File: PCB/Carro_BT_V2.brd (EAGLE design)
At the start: 58 x 71 mm, 7 parts, among them X2 22-23-2041, X3 22-23-2021, X4 22-23-2021

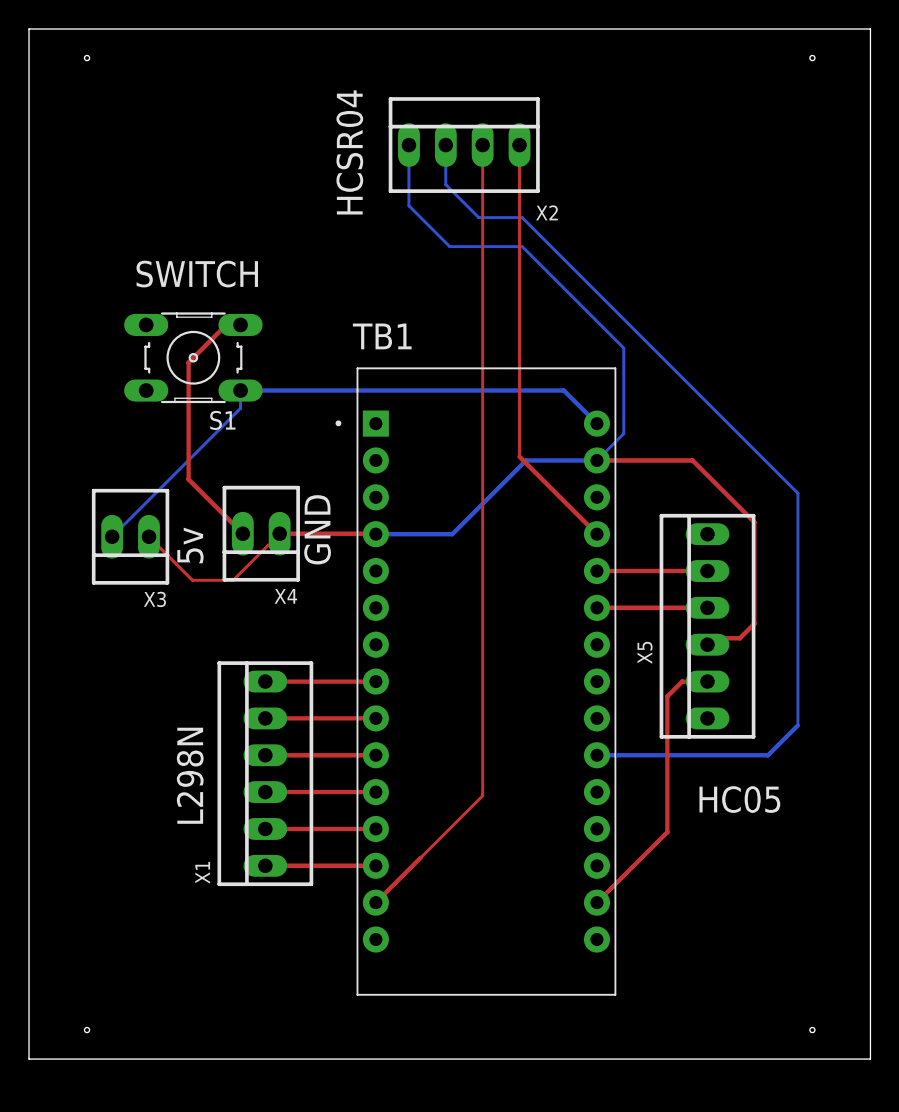
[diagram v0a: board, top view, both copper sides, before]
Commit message: Se reduce el tamaño de la PCB para reducir el precio de fabricación.
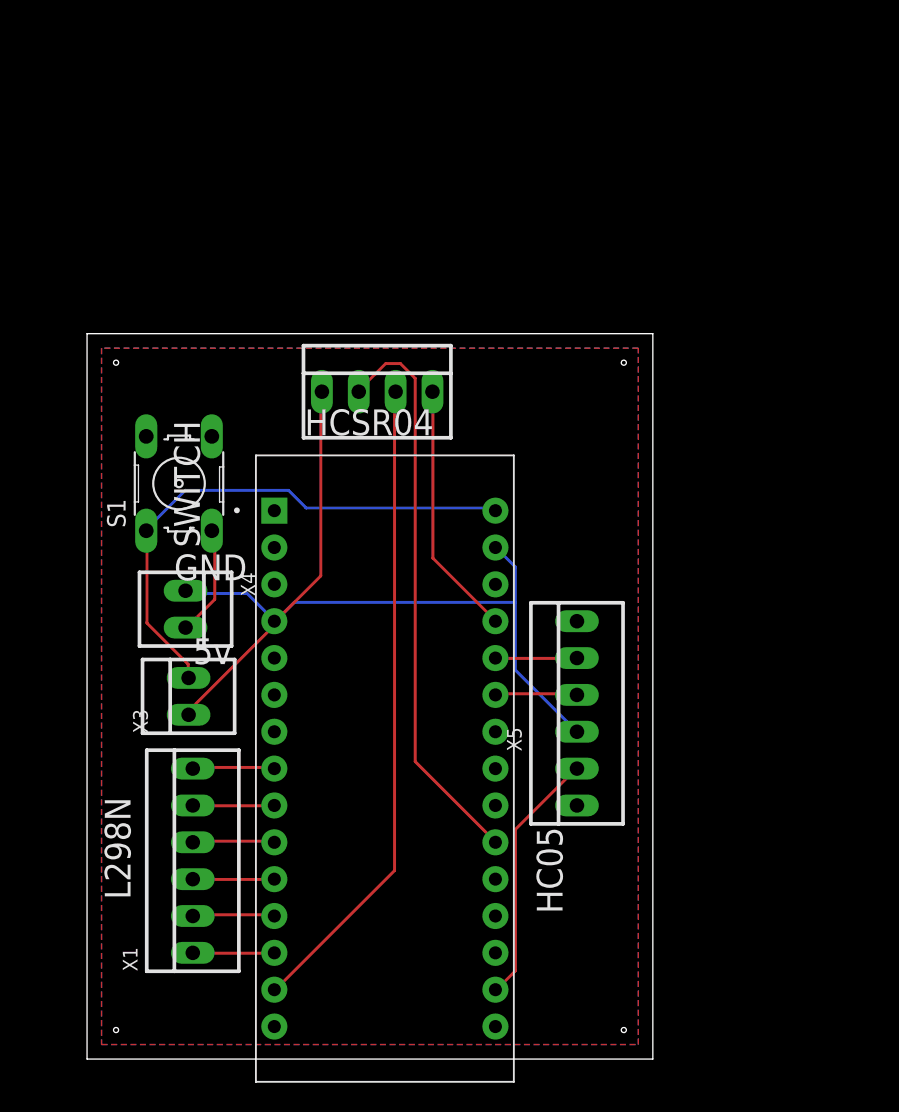
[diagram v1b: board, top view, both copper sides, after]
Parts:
- moved X2 18.0 mm to (24.0, 46.0)
- moved X3 11.7 mm to (11.0, 25.0), turned to 90 degrees
- moved X5 10.8 mm to (37.8, 23.8)
- moved TB1 9.22 mm to (24.5, 20.0)
- moved S1 8.73 mm to (10.3, 39.7), turned to 90 degrees
- moved X1 7.81 mm to (11.3, 13.7)
- moved X4 7.37 mm to (10.8, 31.0), turned to 270 degrees
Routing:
- net ECHO: track 66.5 -> 39.4 mm
- net GND: track 91.7 -> 65.4 mm
- net 5V_HCSR04: track 29.0 -> 17.6 mm
- net TRIG: track 55.3 -> 44.7 mm
- net N$6: track 18.0 -> 7.69 mm
- net VCC: track 39.3 -> 37.3 mm
- net RX_HC05: track 7.62 -> 5.62 mm
- net IN3: track 7.62 -> 5.63 mm
- net IN1: track 7.62 -> 5.63 mm
- net ENB: track 7.62 -> 5.63 mm
- net TX_HC05: track 7.62 -> 5.66 mm
- net IN4: track 7.62 -> 5.70 mm
- net IN2: track 7.62 -> 5.70 mm
- net ENA: track 7.62 -> 5.70 mm
- net 3V3_HC05: track 19.4 -> 17.6 mm
- added copper zone on layer 1, net GND
- added copper zone on layer 16, net GND
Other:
- board size 58 x 71 mm -> 39 x 50 mm
